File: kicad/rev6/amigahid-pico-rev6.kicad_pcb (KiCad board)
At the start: 2 copper layers, 100 x 80 mm, 115 parts, among them J1 A500 KBD OUT, J10 PS/2 KBD OUT, J11 DIN5 KBD IN, J12 PS/2 KBD IN, J13 USB-C AUX 5V, J2 DEBUG UART+SWD, J3 OLED I2C, J4 USB-A HOST, J7 SPARE GP28, J8 A500 KBD IN, J9 DIN5 KBD OUT, P1 DE9 MALE PORT 1, P2 DE9 MALE PORT 2, Q1 BSS138, Q10 BSS138, Q11 BSS138, Q12 BSS138, Q13 BSS138, Q14 BSS138, Q15 BSS138, Q16 BSS138, Q17 BSS138, Q18 BSS138, Q19 BSS138, Q2 BSS138, Q3 BSS138, Q4 BSS138, Q5 BSS138, Q6 BSS138, Q7 BSS138, Q8 BSS138, Q9 BSS138, U1 PicoW, U2 USBLC6-2SC6

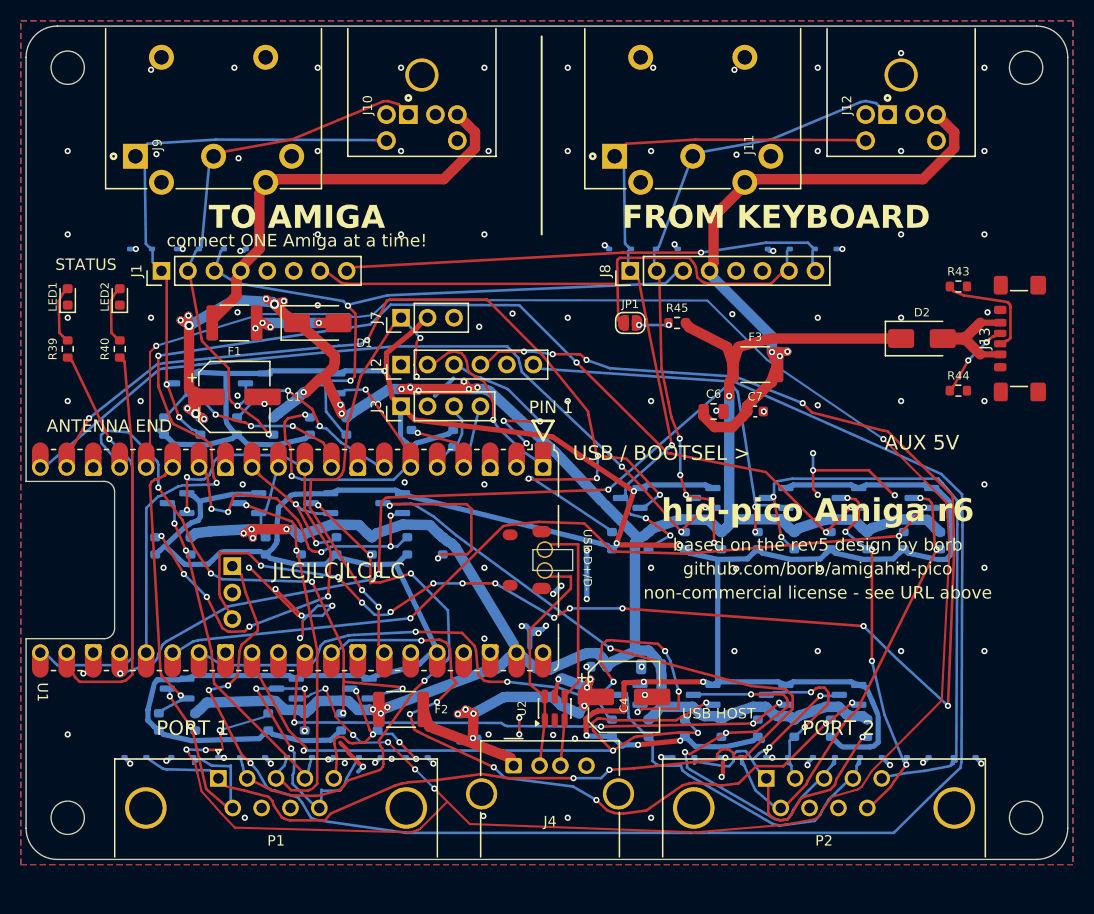
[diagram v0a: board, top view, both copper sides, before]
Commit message: kicad: re-lay the rev6 copper on 45-degree runs
the rev6 tracks came off a grid maze router: electrically right, but laid at
whatever angle got round the next obstacle. check_rev6_style.py has measured
that since it was added and had never passed - 38.416% of the routed length sat
on a multiple of 45 degrees where s1 asks for 99%, with eight ladders of
sub-millimetre jogs on top of it. that gate was authored against copper already
at 34.61% and stayed red through every commit since, so it was never a
regression to fix; the board simply had to be re-laid.

every track is re-laid. the topology is taken from the copper that was already
there - which layer, which via, which pad, which junction - and only the shape
of each node-to-node link is recomputed, on an octilinear grid inside a corridor
around where that link already ran, so nothing wanders further than it has to.
long links are cut into ~9 mm pieces first, which keeps each search local and
keeps the result close to the old course.

two kinds of joint had to be modelled before that was safe. the old router
sometimes finished a run by parking its end on top of another run of the same
net, or reached a via by passing over it rather than ending on it; kicad reads
both as connections and a graph built from endpoints reads them as dead ends, so
re-laying the two sides independently pulls them apart. every such joint is now
given a real shared vertex first. what the router still leaves as a ladder is
replaced afterwards by the octilinear connection between the same two points -
pulled back into, or carried past, the straight runs either side where that is
what it takes - and only kept if it clears everything the old shape cleared and
still covers every pad and every neighbouring run it used to touch.

five ground stitching vias are added, 346 -> 351. re-routing moves where tracks
cross the pours, and these are the pieces of pour that would otherwise no longer
reach the plane: one holds j2's ground pin, another the c2/c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
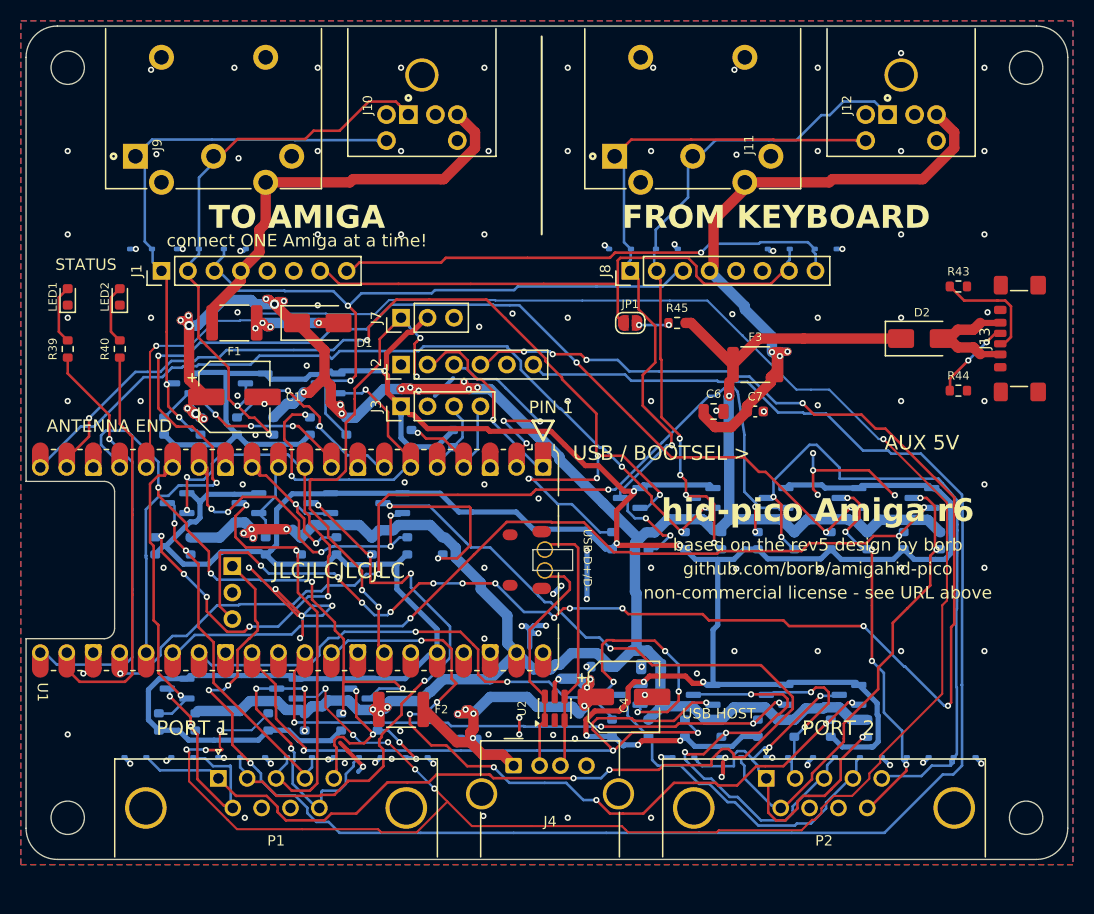
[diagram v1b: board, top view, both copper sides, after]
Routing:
- net +3V3: track 352.8 -> 361.5 mm
- net /KBIN_5V: track 65.1 -> 58.6 mm
- net /SYS5V: track 293.0 -> 299.4 mm
- net /swdio: track 153.0 -> 157.3 mm
- net /swclk: track 167.4 -> 171.2 mm
- net /cont1_vq: track 34.7 -> 38.1 mm
- net /cont1_v: track 127.3 -> 130.6 mm
- net /cont2_b3: track 59.3 -> 62.3 mm
- net /cont2_b3_lo: track 89.2 -> 92.1 mm
- net /cont2_b2_lo: track 111.6 -> 114.4 mm
- net /kbclock: track 53.1 -> 50.3 mm
- net /cont1_b2_lo: track 229.3 -> 232.0 mm
- net /kbin_dat: track 56.8 -> 59.4 mm
- net /cont2_v_lo: track 69.5 -> 72.0 mm
- net /cont1_b3_lo: track 53.7 -> 55.8 mm
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
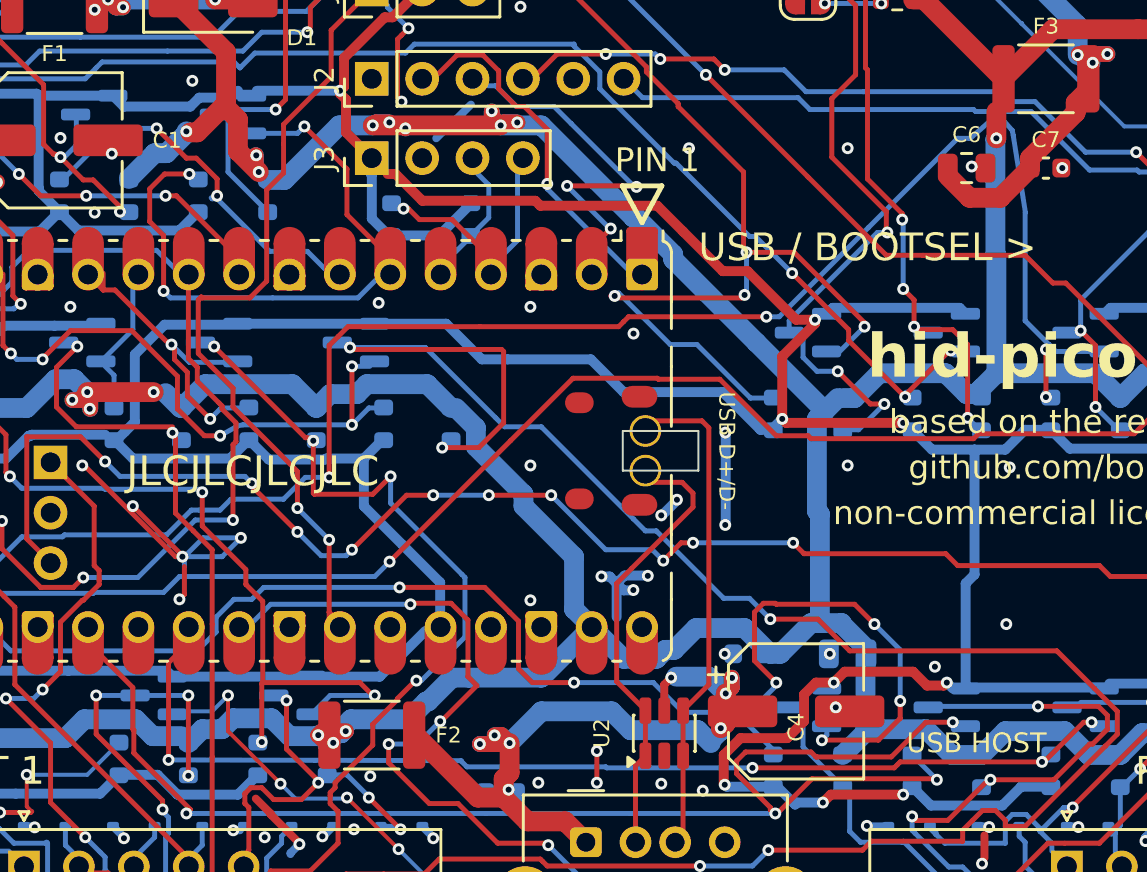
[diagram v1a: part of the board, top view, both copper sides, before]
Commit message: kicad: make the rev6 power netclass live and route the rails to it
net_settings.meta.version was 2 while membership was expressed with
netclass_patterns, which is a v3 construct. on load kicad runs its v2 -> v3
migration, builds membership from classes[*].nets - absent here - and overwrites
the hand-written patterns with the empty result, so every supply rail resolved
to Default and every rev6 drc run recorded in a commit message so far measured
the supply copper against Default's 0.20 mm rather than Power's 0.25 mm. the
netclass has been decorative since f5677cb added it, and the file has been at
version 2 since it was bootstrapped from rev5 at 8811818.

bumping the version to 3 makes it live and turns up 12 clearance errors that
were there all along (7 without --all-track-errors). the board is moved to meet
the rule, not the rule to meet the board:

  - the sys5v exits onto r4.1, r18.1 and r20.1 sat 0.225-0.245 mm off the
    signal runs beneath them. each is pulled 0.05 mm back up its own pad,
    which already stood further off than the copper leaving it did.
  - the sys5v dip onto r12.1 is flattened 0.05 mm higher, on 45s, still
    inside the pad.
  - cont2_b3_lo crosses the top of the sys5v trunk through a 0.7 mm corridor
    between swclk and the trunk's via, and the maze router had left seven
    segments in it, three of them off-45. they become four clean runs, and
    the first millimetre of the trunk necks to 0.8 mm - f2's floor, and no
    real neck, since the via feeding it is 0.6 mm - so the corridor has to be
    0.775 mm wide instead of 0.875 mm. s1 rises 99.525% -> 99.683%, off-angle
    17.366 -> 11.599 mm.

the gnd pours are refilled at the live clearance, which is the bulk of the
board diff.

+3v3 leaves the netclass. it was a member declaring 1.0 mm track width while
routed at 0.5 mm over all 181 of its segments, and f2 already excepted it as a
logic rail - a class whose whole point is wide supply copper cannot also hold
the one rail nobody mea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
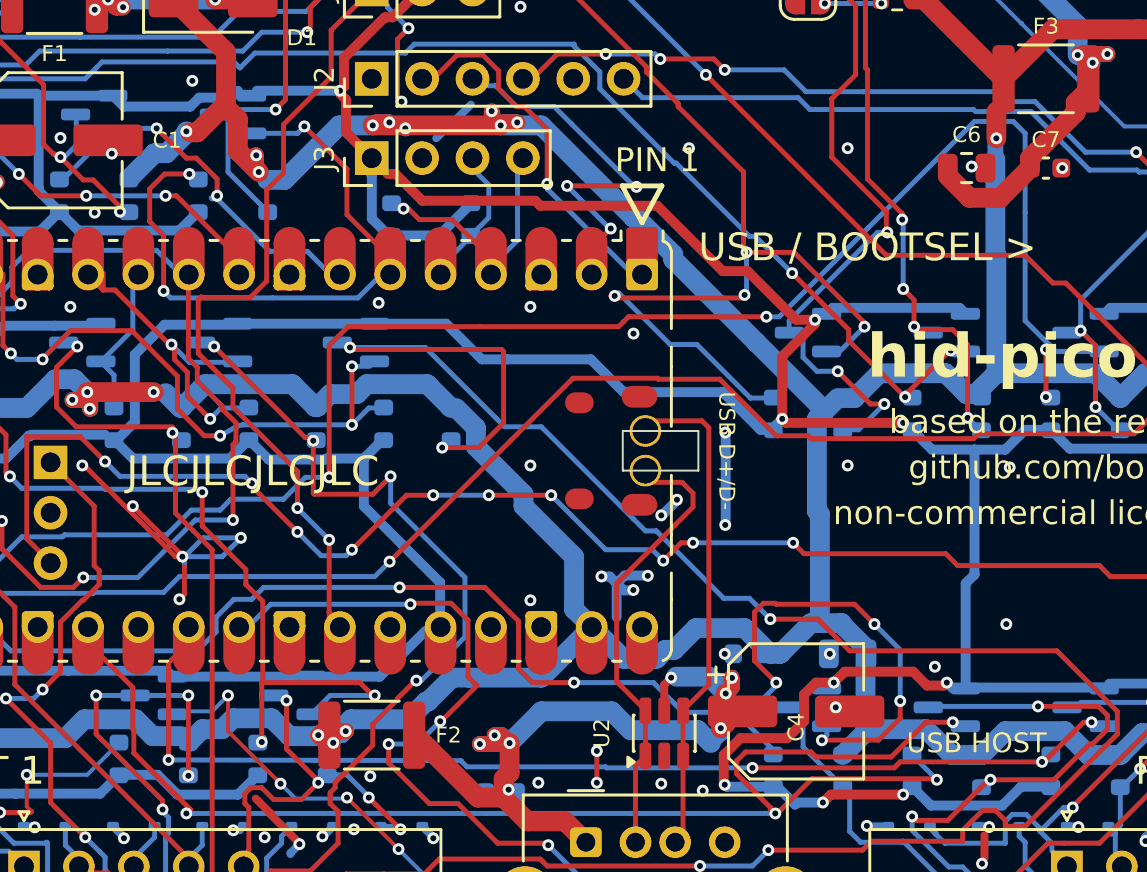
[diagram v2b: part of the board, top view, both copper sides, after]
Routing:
- net /cont2_b3_lo: track 92.1 -> 92.6 mm
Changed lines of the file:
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@@
 	)
 	(segment
+		(start 67.45 36.55)
+		(end 67.45 41.35)
+		(width 1)
+		(layer "B.Cu")
+		(net "/SYS5V")
+	)
+	(segment
 		(start 35.75 47.9)
 		(end 35.25 48.4)
@@
 	)
 	(segment
-		(start 23.75 37.55)
+		(start 23.85 37.45)
 		(end 25.05 36.25)
 		(width 1)
@@
 	(segment
 		(start 34.95 64.8)
-		(end 33.75 66)
+		(end 33.8 65.95)
 		(width 1)
 		(layer "B.Cu")
@@
 	(segment
 		(start 33.9 48.4)
-		(end 33.2 49.1)
+		(end 33.25 49.05)
 		(width 1)
 		(layer "B.Cu")
@@
 		(start 67.5 35.5)
 		(end 67.45 35.55)
-		(width 1)
+		(width 0.8)
 		(layer "B.Cu")
 		(net "/SYS5V")
@@
 	)
 	(segment
+		(start 33.15 49.05)
+		(end 33.25 49.05)
+		(width 1)
+		(layer "B.Cu")
+		(net "/SYS5V")
+	)
+	(segment
 		(start 51.2 41.6)
 		(end 51.2 41.35)
@@
 	(segment
 		(start 32 47.9)
-		(end 33.2 49.1)
+		(end 33.15 49.05)
 		(width 1)
 		(layer "B.Cu")
@@
 	(segment
 		(start 27.45 65.3)
-		(end 26.75 66)
+		(end 26.8 65.95)
 		(width 1)
 		(layer "B.Cu")
@@
 	(segment
 		(start 67.45 35.55)
-		(end 67.45 41.35)
-		(width 1)
+		(end 67.45 36.55)
+		(width 0.8)
 		(layer "B.Cu")
 		(net "/SYS5V")
@@
 	)
 	(segment
-		(start 65.55 35.5)
-		(end 66.2 35.5)
-		(width 0.25)
-		(layer "B.Cu")
-		(net "/cont2_b3_lo")
-	)
-	(segment
 		(start 12.9 60.4)
 		(end 12.9 59.7)
@@
 	)
 	(segment
-		(start 68.3 35.1)
-		(end 68.35 35.35)
-		(width 0.25)
-		(layer "B.Cu")
-		(net "/cont2_b3_lo")
-	)
-	(segment
-		(start 67.1 34.7)
-		(end 67.35 34.65)
-		(width 0.25)
-		(layer "B.Cu")
-		(net "/cont2_b3_lo")
-	)
-	(segment
 		(start 32.65 52.6)
 		(end 33.85 52.6)
@@
 	)
 	(segment
+		(start 68.35 34.65)
+		(end 68.95 35.25)
+		(width 0.25)
+		(layer "B.Cu")
+		(net "/cont2_b3_lo")
+	)
+	(segment
 		(start 28.9 53.7)
 		(end 31.55 53.7)
@@
 	)
 	(segment
-		(start 68.35 35.35)
-		(end 68.964194 39.239898)
-		(width 0.25)
-		(layer "B.Cu")
-		(net "/cont2_b3_lo")
-	)
-	(segment
 		(start 18.35 55.6)
 		(end 20.4 55.6)
@@
 	)
 	(segment
-		(start 67.9 34.65)
-		(end 68.3 35.1)
-		(width 0.25)
-		(layer "B.Cu")
-		(net "/cont2_b3_lo")
-	)
-	(segment
 		(start 31.55 53.7)
 		(end 32.65 52.6)
@@
 	)
 	(segment
+		(start 68.95 35.25)
+		(end 68.95 39.25)
+		(width 0.25)
+		(layer "B.Cu")
+		(net "/cont2_b3_lo")
+	)
+	(segment
 		(start 68.95 39.25)
 		(end 68.95 44.7)
@@
 	)
 	(segment
-		(start 66.176321 35.508219)
-		(end 67.1 34.7)
+		(start 65.55 35.5)
+		(end 66.4 34.65)
+		(width 0.25)
+		(layer "B.Cu")
+		(net "/cont2_b3_lo")
+	)
+	(segment
+		(start 66.4 34.65)
+		(end 68.35 34.65)
 		(width 0.25)
 		(layer "B.Cu")
@@
 		(width 0.25)
 		(layer "B.Cu")
-		(net "/cont2_b3_lo")
-	)
-	(segment
-		(start 67.35 34.65)
-		(end 67.9 34.65)
-		(width 0.25)
-		(layer "B.Cu")

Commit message: kicad: credit r6 and link the fork on the silkscreen
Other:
- board text added: "github.com/jusii/amigahid-pico"
- board text added: "non-commercial license - see URLs above"
- board text added: "r6 by Jusii"
- board text removed: "non-commercial license - see URL above"
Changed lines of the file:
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@@
 		)
 	)
-	(gr_text "based on the rev5 design by borb"
+	(gr_text "r6 by Jusii"
 		(at 76 49.8 0)
 		(layer "F.SilkS")
@@
 		)
 	)
-	(gr_text "github.com/borb/amigahid-pico"
+	(gr_text "github.com/jusii/amigahid-pico"
 		(at 76 52.1 0)
 		(layer "F.SilkS")
@@
 		)
 	)
-	(gr_text "non-commercial license - see URL above"
+	(gr_text "based on the rev5 design by borb"
 		(at 76 54.4 0)
 		(layer "F.SilkS")
 		(effects
+			(font
+				(size 1.2 1.2)
+				(thickness 0.2)
+			)
+		)
+	)
+	(gr_text "github.com/borb/amigahid-pico"
+		(at 76 56.7 0)
+		(layer "F.SilkS")
+		(effects
+			(font
+				(size 1.2 1.2)
+				(thickness 0.2)
+			)
+		)
+	)
+	(gr_text "non-commercial license - see URLs above"
+		(at 76 59 0)
+		(layer "F.SilkS")
+		(effects

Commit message: kicad: rename the board to ux, drop the unsupported license line
silkscreen title is now "hid-pico Amiga UX", revision line "UX rev 1 - by
Jusii". the license assertion is removed: neither repo carries a license
file and both readmes point at epl-2.0 (tentative), so the board no longer
claims what no document supports. checker H2 re-targeted from the r6
marker to the UX product/revision marker in the same commit. the de9
footprint gains the verify-against-sample marker and the p1/p2 sourcing
fields get the corrected caliper dimensions (near pin row 7.78 mm, flange
holes 4.94 mm).
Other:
- board text added: "UX rev 1 - by Jusii"
- board text added: "hid-pico Amiga UX"
- board text removed: "hid-pico Amiga r6"
- board text removed: "non-commercial license - see URLs above"
- board text removed: "r6 by Jusii"
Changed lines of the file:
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@@
 			)
 		)
-		(property "Sourcing" "Power Dynamics PDI-09S-5 (DE9 male, right-angle THT, 5.0 mm footprint: near pin row 4.94 mm from the board edge, 2 x 3.2 mm holes on 25.0 mm centres; 7.2 mm / 0.318 in parts do NOT fit) - hand-solder, not JLC-assembled"
+		(property "Sourcing" "Power Dynamics PDI-09S-5 (DE9 male, right-angle THT, 5.34 mm footprint family: flange-screw holes 2 x 3.2 mm on 25.0 mm centres THROUGH the pcb at 4.94 mm from the board edge, near pin row 7.78 mm from the edge; 9.4 mm European-footprint and 7.2/8.08 mm parts do NOT fit) - hand-solder, not JLC-assembled"
 			(at 0 0 0)
 			(layer "F.Fab")
@@
 			)
 		)
-		(property "Sourcing" "Power Dynamics PDI-09S-5 (DE9 male, right-angle THT, 5.0 mm footprint: near pin row 4.94 mm from the board edge, 2 x 3.2 mm holes on 25.0 mm centres; 7.2 mm / 0.318 in parts do NOT fit) - hand-solder, not JLC-assembled"
+		(property "Sourcing" "Power Dynamics PDI-09S-5 (DE9 male, right-angle THT, 5.34 mm footprint family: flange-screw holes 2 x 3.2 mm on 25.0 mm centres THROUGH the pcb at 4.94 mm from the board edge, near pin row 7.78 mm from the edge; 9.4 mm European-footprint and 7.2/8.08 mm parts do NOT fit) - hand-solder, not JLC-assembled"
 			(at 0 0 0)
 			(layer "F.Fab")
@@
 		)
 	)
-	(gr_text "r6 by Jusii"
+	(gr_text "UX rev 1 - by Jusii"
 		(at 76 49.8 0)
 		(layer "F.SilkS")
@@
 		)
 	)
-	(gr_text "non-commercial license - see URLs above"
-		(at 76 59 0)
-		(layer "F.SilkS")
-		(effects
-			(font
-				(size 1.2 1.2)
-				(thickness 0.2)
-			)
-		)
-	)
 	(gr_text "PORT 1"
 		(at 16 67.4 0)
@@
 		)
 	)
-	(gr_text "hid-pico Amiga r6"
+	(gr_text "hid-pico Amiga UX"
 		(at 76 46.5 0)
 		(layer "F.SilkS")
